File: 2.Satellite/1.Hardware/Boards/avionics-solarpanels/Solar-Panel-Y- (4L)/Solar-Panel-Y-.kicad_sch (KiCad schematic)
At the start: 61 parts, among them J1 FTS-107-01-X-DV-A, J2 BM02B-SRSS-TB, SW1 D2F-L2-A1, SW2 D2F-L2-A, U1 BQ25570RGRR, U2 OPT3001, U3 MAX40200AUK

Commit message: update BOM
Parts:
- C1: Manufacturer_Name (none) -> KYOCERA AVX; Manufacturer_Part_Number (none) -> 04025C104KAT2A; Package/Footprint (none) -> 0402; Website (none) -> https://www.digikey.pt/pt/products/detail/kyocera-avx/KGM05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
- C10, C11, C2, C9: Manufacturer_Name (none) -> KYOCERA AVX; Manufacturer_Part_Number (none) -> 06035C104K4T2A; Package/Footprint (none) -> 0603; Website (none) -> https://www.digikey.pt/pt/products/detail/kyocera-avx/KAM15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
- C3, C7: Manufacturer_Name (none) -> Murata Electronics; Manufacturer_Part_Number (none) -> GRT188R6YA475KE13D; Package/Footprint (none) -> 0603; Website (none) -> https://www.digikey.pt/pt/products/detail/murata-electronic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
- C4: Manufacturer_Name (none) -> KYOCERA AVX; Manufacturer_Part_Number (none) -> 06031C103K4T4A; Package/Footprint (none) -> 0603; Website (none) -> https://www.digikey.pt/pt/products/detail/kyocera-avx/KAM15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
- C5: Manufacturer_Name (none) -> Murata Electronics; Manufacturer_Part_Number (none) -> GRM21BR60J107ME15K; Package/Footprint (none) -> 0805; Website (none) -> https://www.digikey.pt/pt/products/detail/murata-electronic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
- C6: Manufacturer_Name (none) -> Murata Electronics; Manufacturer_Part_Number (none) -> GRT188R61H105KE13D; Package/Footprint (none) -> 0603; Website (none) -> https://www.digikey.pt/pt/products/detail/murata-electronic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
- C8: Manufacturer_Name (none) -> Murata Electronics; Manufacturer_Part_Number (none) -> GRT188R61A226ME13D; Package/Footprint (none) -> 0603; Website (none) -> https://www.digikey.pt/pt/products/detail/murata-electronic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
- D1: Manufacturer_Name (none) -> onsemi; Manufacturer_Part_Number (none) -> SZMM5Z5V1T1G; Package/Footprint (none) -> SOD-523; Website (none) -> https://www.digikey.pt/pt/products/detail/onsemi/SZMM5Z5V1T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
- D2, D3, D4: Manufacturer_Name (none) -> Diodes Incorporated; Manufacturer_Part_Number (none) -> DFLS130L-7; Package/Footprint (none) -> PowerDI-123; Website (none) -> https://www.digikey.pt/pt/products/detail/diodes-incorporat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
- J1: Manufacturer_Name (none) -> Samtec Inc.; Manufacturer_Part_Number (none) -> FTS-107-01-L-DV-A; Website (none) -> https://www.digikey.pt/pt/products/detail/samtec-inc/FTS-10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
- J2: Manufacturer_Name (none) -> JST Sales America Inc.; Manufacturer_Part_Number (none) -> BM02B-SRSS-TB(LF)(SN); Website (none) -> https://www.digikey.pt/pt/products/detail/jst-sales-america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
- L1: Manufacturer_Name (none) -> Coilcraft; Manufacturer_Part_Number (none) -> LPS4018-223MRC; Package/Footprint (none) -> 1515; Website (none) -> https://www.digikey.pt/pt/products/detail/coilcraft/LPS4018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
- L2: Manufacturer_Name (none) -> Coilcraft; Manufacturer_Part_Number (none) -> LPS4018-103MRC; Package/Footprint (none) -> 1515; Website (none) -> https://www.digikey.pt/pt/products/detail/coilcraft/LPS4018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
- R1, R2: Manufacturer_Name (none) -> Stackpole Electronics Inc; Manufacturer_Part_Number (none) -> RMCF0402ZT0R00; Package/Footprint (none) -> 0402; Website (none) -> https://www.digikey.pt/pt/products/detail/stackpole-electro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
- R10, R8: Manufacturer_Name (none) -> Vishay Dale; Manufacturer_Part_Number (none) -> CRCW06038M25FKEA; Package/Footprint (none) -> 0603; Website (none) -> https://www.digikey.pt/pt/products/detail/vishay-dale/CRCW0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
- R11: Manufacturer_Name (none) -> Stackpole Electronics Inc; Manufacturer_Part_Number (none) -> RMCF0603FT4M75; Package/Footprint (none) -> 0603; Website (none) -> https://www.digikey.pt/pt/products/detail/stackpole-electro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
- R12, R13, R16, R17, R18, R3, R31, R4: Manufacturer_Name (none) -> Stackpole Electronics Inc; Manufacturer_Part_Number (none) -> RMCF0603ZT0R00; Package/Footprint (none) -> 0603; Website (none) -> https://www.digikey.pt/pt/products/detail/stackpole-electro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
- R5: Manufacturer_Name (none) -> Stackpole Electronics Inc; Manufacturer_Part_Number (none) -> RMCF0603FT7M32; Package/Footprint (none) -> 0603; Website (none) -> https://www.digikey.pt/pt/products/detail/stackpole-electro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
- R6: Manufacturer_Name (none) -> Stackpole Electronics Inc; Manufacturer_Part_Number (none) -> RMCF0603FT5M62; Package/Footprint (none) -> 0603; Website (none) -> https://www.digikey.pt/pt/products/detail/stackpole-electro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
- R7: Manufacturer_Name (none) -> Stackpole Electronics Inc; Manufacturer_Part_Number (none) -> RMCF0603FT374K; Package/Footprint (none) -> 0603; Website (none) -> https://www.digikey.pt/pt/products/detail/stackpole-electro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
- R9: Manufacturer_Name (none) -> Stackpole Electronics Inc; Manufacturer_Part_Number (none) -> RMCF0603FT4M53; Package/Footprint (none) -> 0603; Website (none) -> https://www.digikey.pt/pt/products/detail/stackpole-electro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
- SC1, SC2, SC3, SC4, SC5, SC6, SC7, SC8: Manufacturer_Name (none) -> ANYSOLAR Ltd; Manufacturer_Part_Number (none) -> KXOB25-05X3F-TR; Website (none) -> https://www.digikey.pt/pt/products/detail/anysolar-ltd/KXOB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
- SW1: Manufacturer_Name (none) -> Omron Electronics Inc-EMC Div; Manufacturer_Part_Number (none) -> D2F-L2-A1; Website (none) -> https://www.digikey.pt/pt/products/detail/omron-electronics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
- SW2: Manufacturer_Name (none) -> Omron Electronics Inc-EMC Div; Manufacturer_Part_Number (none) -> D2F-L2-A; Website (none) -> https://www.digikey.pt/pt/products/detail/omron-electronics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
- U1: Manufacturer_Name (none) -> Texas Instruments; Manufacturer_Part_Number (none) -> BQ25570RGRR; Package/Footprint (none) -> 20-VQFN; Website (none) -> https://www.digikey.pt/pt/products/detail/texas-instruments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
- U2: Manufacturer_Name (none) -> Texas Instruments; Manufacturer_Part_Number (none) -> OPT3001IDNPRQ1; Package/Footprint (none) -> 6-USON; Website (none) -> https://www.digikey.pt/pt/products/detail/texas-instruments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
- U3: Manufacturer_Name (none) -> Analog Devices Inc./Maxim Integrated; Manufacturer_Part_Number (none) -> MAX40200AUK+T; Package/Footprint (none) -> SOT-23-5; Website (none) -> https://www.digikey.pt/pt/products/detail/analog-devices-in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

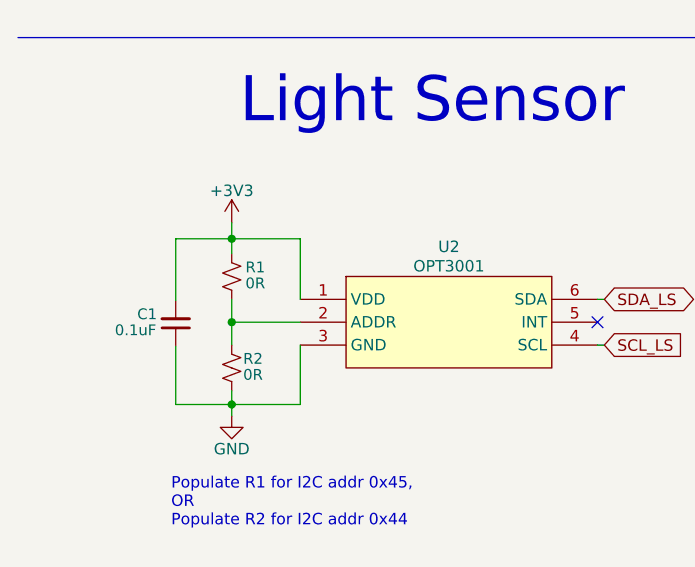
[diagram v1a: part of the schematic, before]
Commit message: Updated I2C address resistors; Added reference to KiCad docs
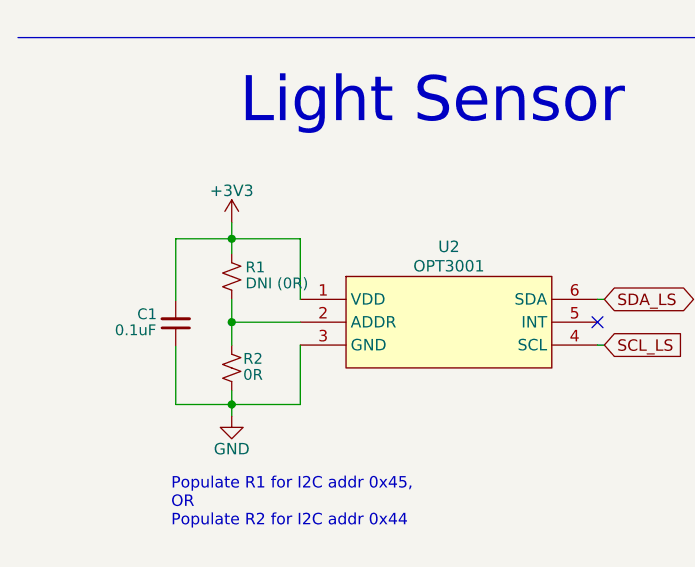
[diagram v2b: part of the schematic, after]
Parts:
- R1: value 0R -> DNI (0R); DNI (none) -> DNI
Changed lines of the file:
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@@
       (effects (font (size 1.2 1.2)) (justify right))
     )
-    (property "Value" "0R" (at 37.211 172.339 0)
+    (property "Value" "DNI (0R)" (at 37.211 172.339 0)
       (effects (font (size 1.2 1.2)) (justify right))
     )
@@
       (effects (font (size 1.27 1.27)) hide)
     )
+    (property "DNI" "DNI" (at 35.687 171.577 0)
+      (effects (font (size 1.27 1.27)) hide)
+    )
